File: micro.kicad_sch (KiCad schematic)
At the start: 0 parts

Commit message: added mcu to schematics
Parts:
- added U1: ~, symbol sumo-robot-symbols:MSP430G2553IPW28
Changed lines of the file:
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@@
 	(generator_version "9.0")
 	(paper "A4")
+	(symbol
+		(lib_id "sumo-robot-symbols:MSP430G2553IPW28")
+		(at 137.16 102.87 0)
+		(unit 1)
+		(exclude_from_sim no)
+		(in_bom yes)
+		(on_board yes)
+		(dnp no)
+		(fields_autoplaced yes)
+		(property "Reference" "U1"
+			(at 158.115 60.96 0)
+			(effects
+				(font
+					(size 1.27 1.27)
+				)
+			)
+		)
+		(property "Value" "~"
+			(at 158.115 63.5 0)
+			(effects
+				(font
+					(size 1.27 1.27)
+				)
+			)
+		)
+		(property "Footprint" ""
+			(at 137.16 102.87 0)
+			(effects
+				(font
+					(size 1.27 1.27)
+				)
+				(hide yes)
+			)
+		)
+		(property "Datasheet" ""
+			(at 137.16 102.87 0)
+			(effects
+				(font
+					(size 1.27 1.27)
+				)
+				(hide yes)
+			)
+		)
+		(property "Description" ""
+			(at 137.16 102.87 0)
+			(effects
+				(font
+					(size 1.27 1.27)
+				)
+				(hide yes)
+			)
+		)
+		(pin "5"
+		)
+		(pin "8"
+		)
+		(pin "3"
+		)
+		(pin "1"
+		)
+		(pin "7"
+		)
+		(pin "20"
+		)
+		(pin "16"
+		)
+		(pin "4"
+		)
+		(pin "26"
+		)
+		(pin "14"
+		)
+		(pin "9"
+		)
+		(pin "25"
+		)
+		(pin "24"
+		)
+		(pin "12"
+		)
+		(pin "2"
+		)
+		(pin "6"
+		)
+		(pin "13"
+		)
+		(pin "28"
+		)
+		(pin "27"
+		)
+		(pin "22"
+		)
+		(pin "19"
+		)
+		(pin "18"
+		)
+		(pin "17"
+		)
+		(pin "23"
+		)
+		(pin "21"
+		)
+		(pin "11"
+		)
+		(pin "10"
+		)
+		(pin "15"
+		)
+		(instances
+			(project ""
+				(path "/f283bc71-7763-4093-b75c-cbe2f5868c12/9428f158-f7fc-4e4a-b97b-e16df299d57c"
+					(reference "U1")
+					(unit 1)
+				)
+			)
+		)
+	)
 )

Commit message: updated poer and range sensor scheamtics
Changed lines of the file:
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@@
 	(generator_version "9.0")
 	(paper "A4")
+	(text_box "There would be some flags coming from the pins to indicate that sensors are active "
+		(exclude_from_sim no)
+		(at 96.52 40.64 0)
+		(size 19.05 17.78)
+		(margins 0.9525 0.9525 0.9525 0.9525)
+		(stroke
+			(width 0)
+			(type solid)
+		)
+		(fill
+			(type none)
+		)
+		(effects
+			(font
+				(size 1.27 1.27)
+			)
+			(justify left top)
+		)
+	)
 	(symbol
 		(lib_id "sumo-robot-symbols:MSP430G2553IPW28")
@@
 		(on_board yes)
 		(dnp no)
-		(fields_autoplaced yes)
 		(property "Reference" "U1"
-			(at 158.115 60.96 0)
+			(at 157.988 63.246 0)
 			(effects
 				(font

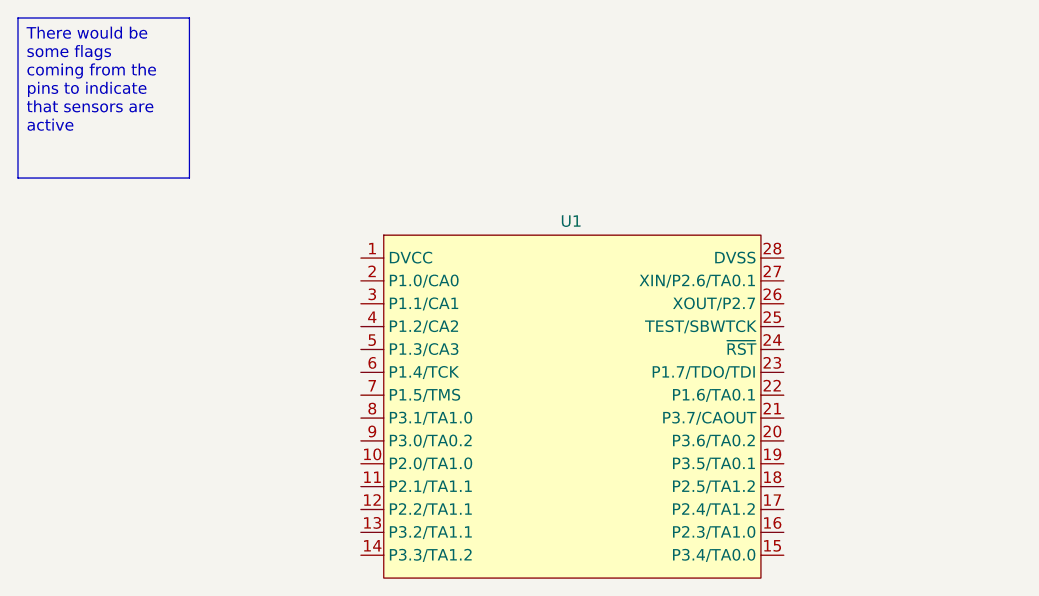
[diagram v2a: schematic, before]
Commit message: added I2C lines
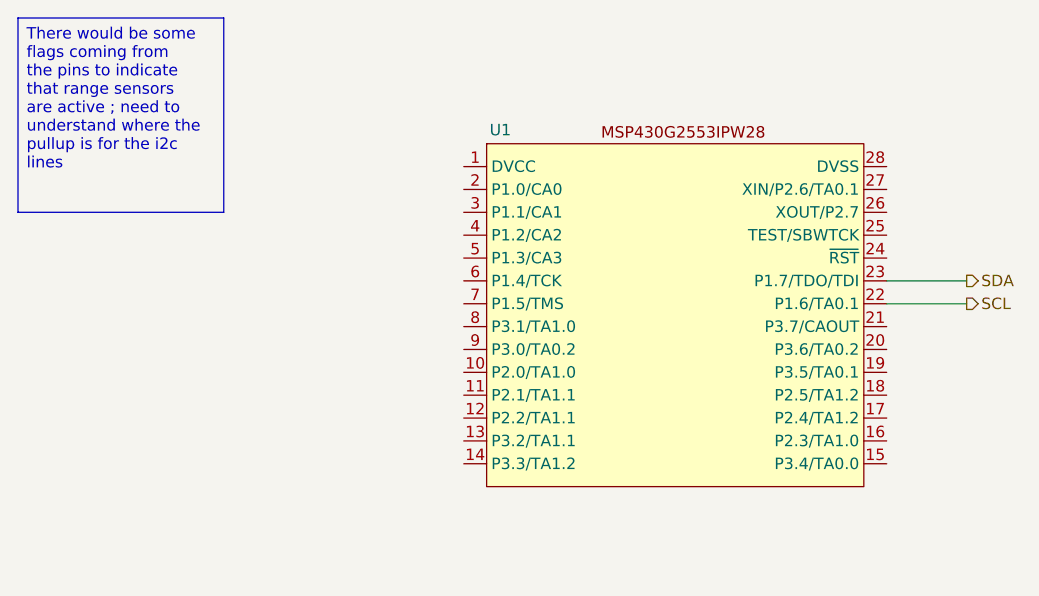
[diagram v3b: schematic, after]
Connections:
- net SCL: now reaches U1.22 (P1.6/TA0.1)
- net SDA: now reaches U1.23 (P1.7/TDO/TDI)
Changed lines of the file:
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@@
 	(generator_version "9.0")
 	(paper "A4")
-	(text_box "There would be some flags coming from the pins to indicate that sensors are active "
+	(text_box "There would be some flags coming from the pins to indicate that range sensors are active ; need to understand where the pullup is for the i2c lines "
 		(exclude_from_sim no)
 		(at 96.52 40.64 0)
-		(size 19.05 17.78)
+		(size 22.86 21.59)
 		(margins 0.9525 0.9525 0.9525 0.9525)
 		(stroke
@@
 		)
 	)
+	(wire
+		(pts
+			(xy 193.04 72.39) (xy 201.93 72.39)
+		)
+		(stroke
+			(width 0)
+			(type default)
+		)
+	)
+	(wire
+		(pts
+			(xy 193.04 69.85) (xy 201.93 69.85)
+		)
+		(stroke
+			(width 0)
+			(type default)
+		)
+	)
+	(hierarchical_label "SCL"
+		(shape output)
+		(at 201.93 72.39 0)
+		(effects
+			(font
+				(size 1.27 1.27)
+			)
+			(justify left)
+		)
+	)
+	(hierarchical_label "SDA"
+		(shape output)
+		(at 201.93 69.85 0)
+		(effects
+			(font
+				(size 1.27 1.27)
+			)
+			(justify left)
+		)
+	)
 	(symbol
 		(lib_id "sumo-robot-symbols:MSP430G2553IPW28")
-		(at 137.16 102.87 0)
+		(at 148.59 92.71 0)
 		(unit 1)
 		(exclude_from_sim no)
@@
 		(dnp no)
 		(property "Reference" "U1"
-			(at 157.988 63.246 0)
+			(at 150.114 53.086 0)
 			(effects
 				(font
@@
 		)
 		(property "Value" "~"
-			(at 158.115 63.5 0)
+			(at 169.545 50.8 0)
 			(effects
 				(font
@@
 		)
 		(property "Footprint" ""
-			(at 137.16 102.87 0)
+			(at 148.59 92.71 0)
 			(effects
 				(font
@@
 		)
 		(property "Datasheet" ""
-			(at 137.16 102.87 0)
+			(at 148.59 92.71 0)
 			(effects
 				(font
@@
 		)
 		(property "Description" ""
-			(at 137.16 102.87 0)
+			(at 148.59 92.71 0)
 			(effects
 				(font
@@
 			)
 		)
-		(pin "5"
+		(pin "1"
+		)
+		(pin "24"
+		)
+		(pin "14"
+		)
+		(pin "6"
+		)
+		(pin "18"
+		)
+		(pin "16"
+		)
+		(pin "7"
+		)
+		(pin "9"
 		)
 		(pin "8"
 		)
+		(pin "4"
+		)
+		(pin "13"
+		)
+		(pin "27"
+		)
+		(pin "5"
+		)
+		(pin "10"
+		)
+		(pin "11"
+		)
+		(pin "26"
+		)
+		(pin "12"
+		)
+		(pin "28"
+		)
+		(pin "25"
+		)
 		(pin "3"
 		)
-		(pin "1"
+		(pin "23"
 		)
-		(pin "7"
+		(pin "2"
+		)
+		(pin "22"
+		)
+		(pin "21"
 		)
 		(pin "20"
 		)
-		(pin "16"
-		)
-		(pin "4"
-		)
-		(pin "26"
-		)
-		(pin "14"
-		)
-		(pin "9"
-		)
-		(pin "25"
-		)
-		(pin "24"
-		)
-		(pin "12"
-		)
-		(pin "2"
-		)
-		(pin "6"
-		)
-		(pin "13"
-		)
-		(pin "28"
-		)
-		(pin "27"
-		)
-		(pin "22"
-		)
 		(pin "19"
-		)
-		(pin "18"
 		)
 		(pin "17"
 		)
-		(pin "23"
-		)
-		(pin "21"
-		)
-		(pin "11"
-		)
-		(pin "10"
-		)
 		(pin "15"

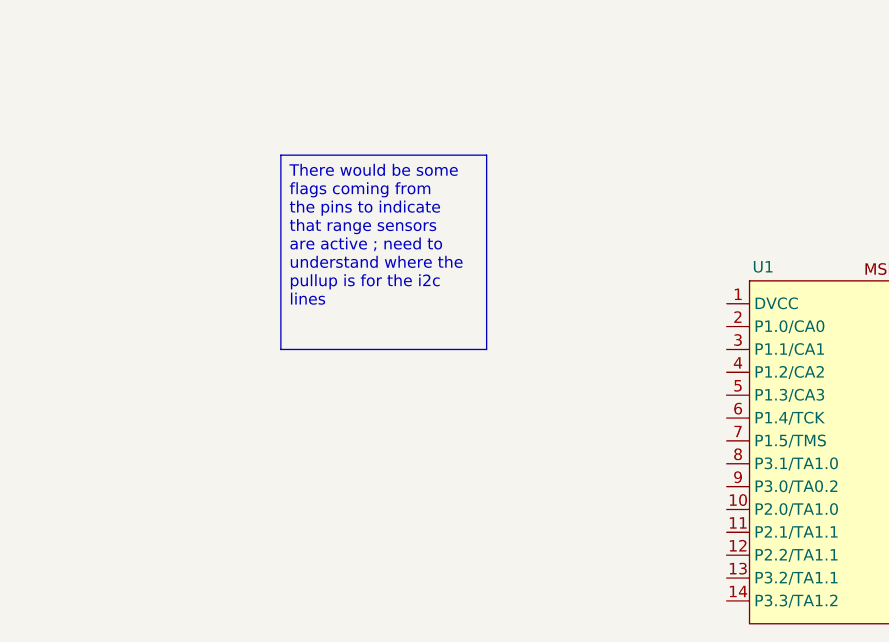
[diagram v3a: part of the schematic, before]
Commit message: added IR receiver circuit
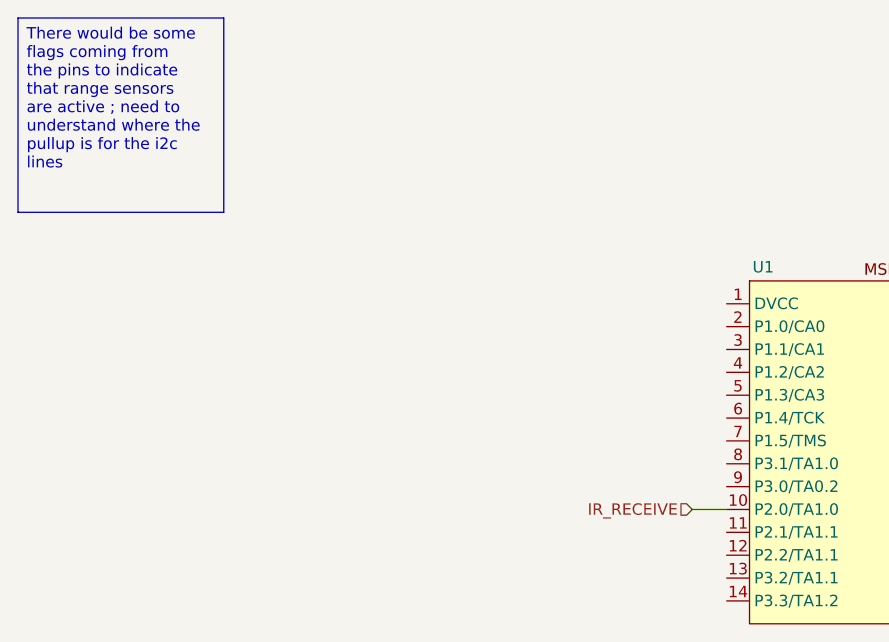
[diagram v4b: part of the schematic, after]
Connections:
- net IR_RECEIVE: now reaches U1.10 (P2.0/TA1.0)
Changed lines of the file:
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@@
 	(text_box "There would be some flags coming from the pins to indicate that range sensors are active ; need to understand where the pullup is for the i2c lines "
 		(exclude_from_sim no)
-		(at 96.52 40.64 0)
+		(at 67.31 25.4 0)
 		(size 22.86 21.59)
 		(margins 0.9525 0.9525 0.9525 0.9525)
@@
 			)
 			(justify left top)
+		)
+	)
+	(wire
+		(pts
+			(xy 142.24 80.01) (xy 146.05 80.01)
+		)
+		(stroke
+			(width 0)
+			(type default)
 		)
 	)
@@
 		)
 	)
+	(hierarchical_label "IR_RECEIVE"
+		(shape input)
+		(at 142.24 80.01 180)
+		(effects
+			(font
+				(size 1.27 1.27)
+			)
+			(justify right)
+		)
+	)

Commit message: added more details to schematics
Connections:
- net LD_FRONT_LEFT: now reaches U1.5 (P1.3/CA3)
- net LD_BACK_LEFT: now reaches U1.6 (P1.4/TCK)
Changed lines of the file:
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@@
 	(wire
 		(pts
-			(xy 193.04 72.39) (xy 201.93 72.39)
+			(xy 142.24 67.31) (xy 146.05 67.31)
 		)
 		(stroke
@@
 	(wire
 		(pts
-			(xy 193.04 69.85) (xy 201.93 69.85)
+			(xy 193.04 72.39) (xy 199.39 72.39)
 		)
 		(stroke
 			(width 0)
 			(type default)
+		)
+	)
+	(wire
+		(pts
+			(xy 142.24 69.85) (xy 146.05 69.85)
+		)
+		(stroke
+			(width 0)
+			(type default)
+		)
+	)
+	(wire
+		(pts
+			(xy 193.04 69.85) (xy 199.39 69.85)
+		)
+		(stroke
+			(width 0)
+			(type default)
+		)
+	)
+	(hierarchical_label "LD_FRONT_LEFT"
+		(shape input)
+		(at 142.24 67.31 180)
+		(effects
+			(font
+				(size 1.27 1.27)
+			)
+			(justify right)
 		)
 	)
@@
 	(hierarchical_label "SCL"
 		(shape output)
-		(at 201.93 72.39 0)
+		(at 199.39 72.39 0)
+		(effects
+			(font
+				(size 1.27 1.27)
+			)
+			(justify left)
+		)
+	)
+	(hierarchical_label "LD_BACK_RIGHT"
+		(shape input)
+		(at 245.11 146.05 90)
 		(effects
 			(font
@@
 	(hierarchical_label "SDA"
 		(shape output)
-		(at 201.93 69.85 0)
+		(at 199.39 69.85 0)
 		(effects
 			(font
@@
 		)
 	)
+	(hierarchical_label "LD_FRONT_RIGHT"
+		(shape input)
+		(at 184.15 144.78 90)
+		(effects
+			(font
+				(size 1.27 1.27)
+			)
+			(justify left)
+		)
+	)
+	(hierarchical_label "LD_BACK_LEFT"
+		(shape input)
+		(at 142.24 69.85 180)
+		(effects
+			(font
+				(size 1.27 1.27)
+			)
+			(justify right)
+		)
+	)

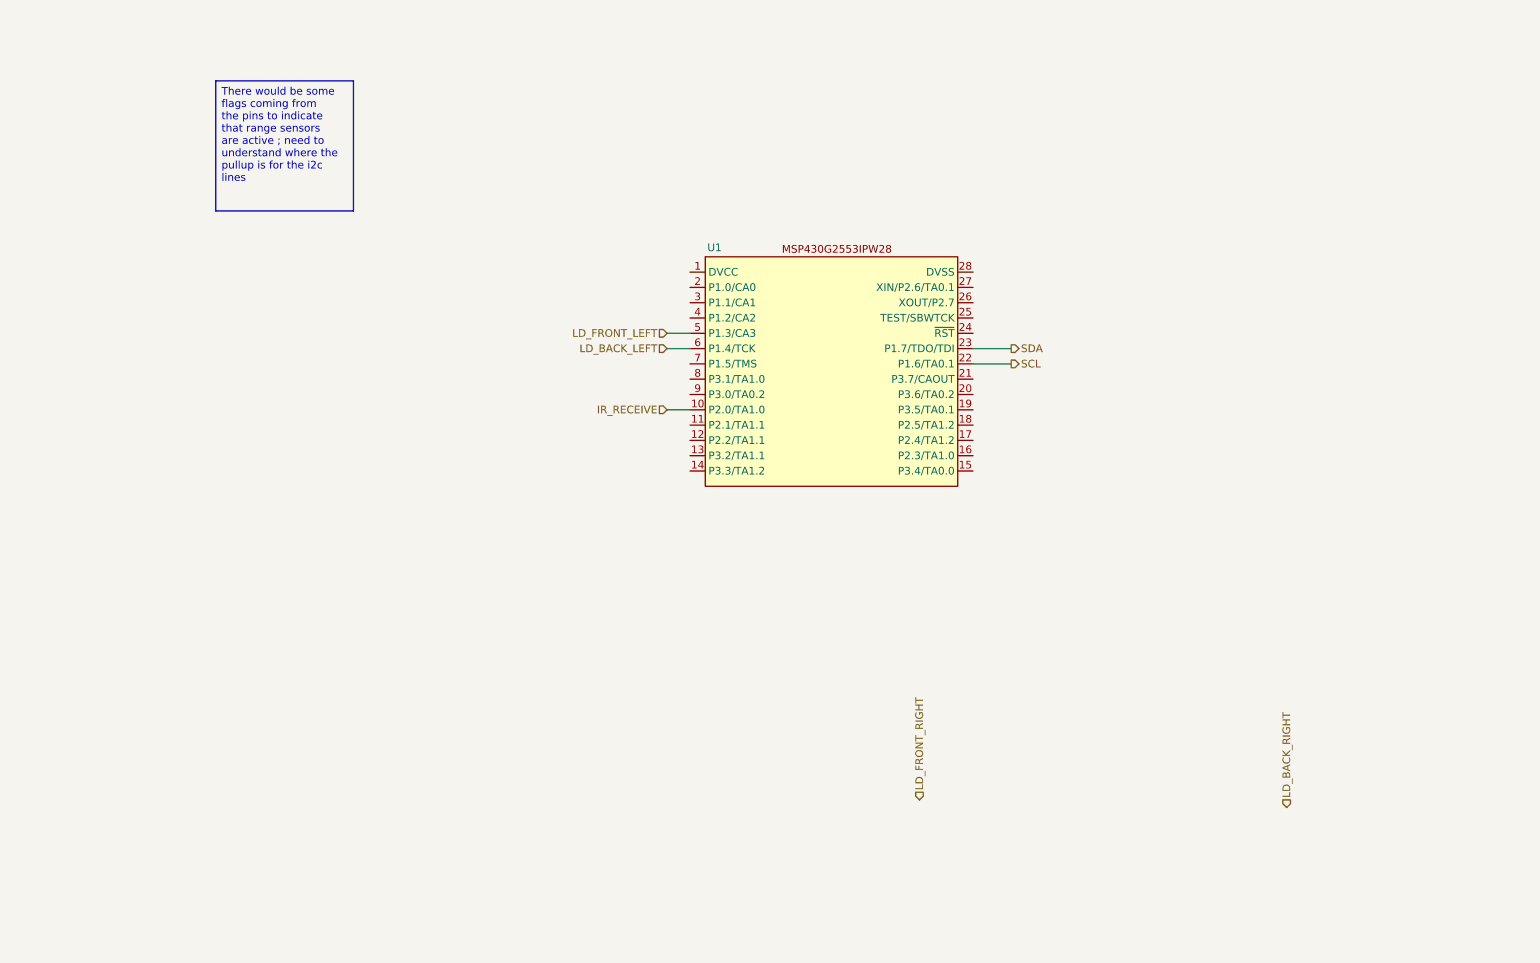
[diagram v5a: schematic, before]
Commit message: updated logic for MCU
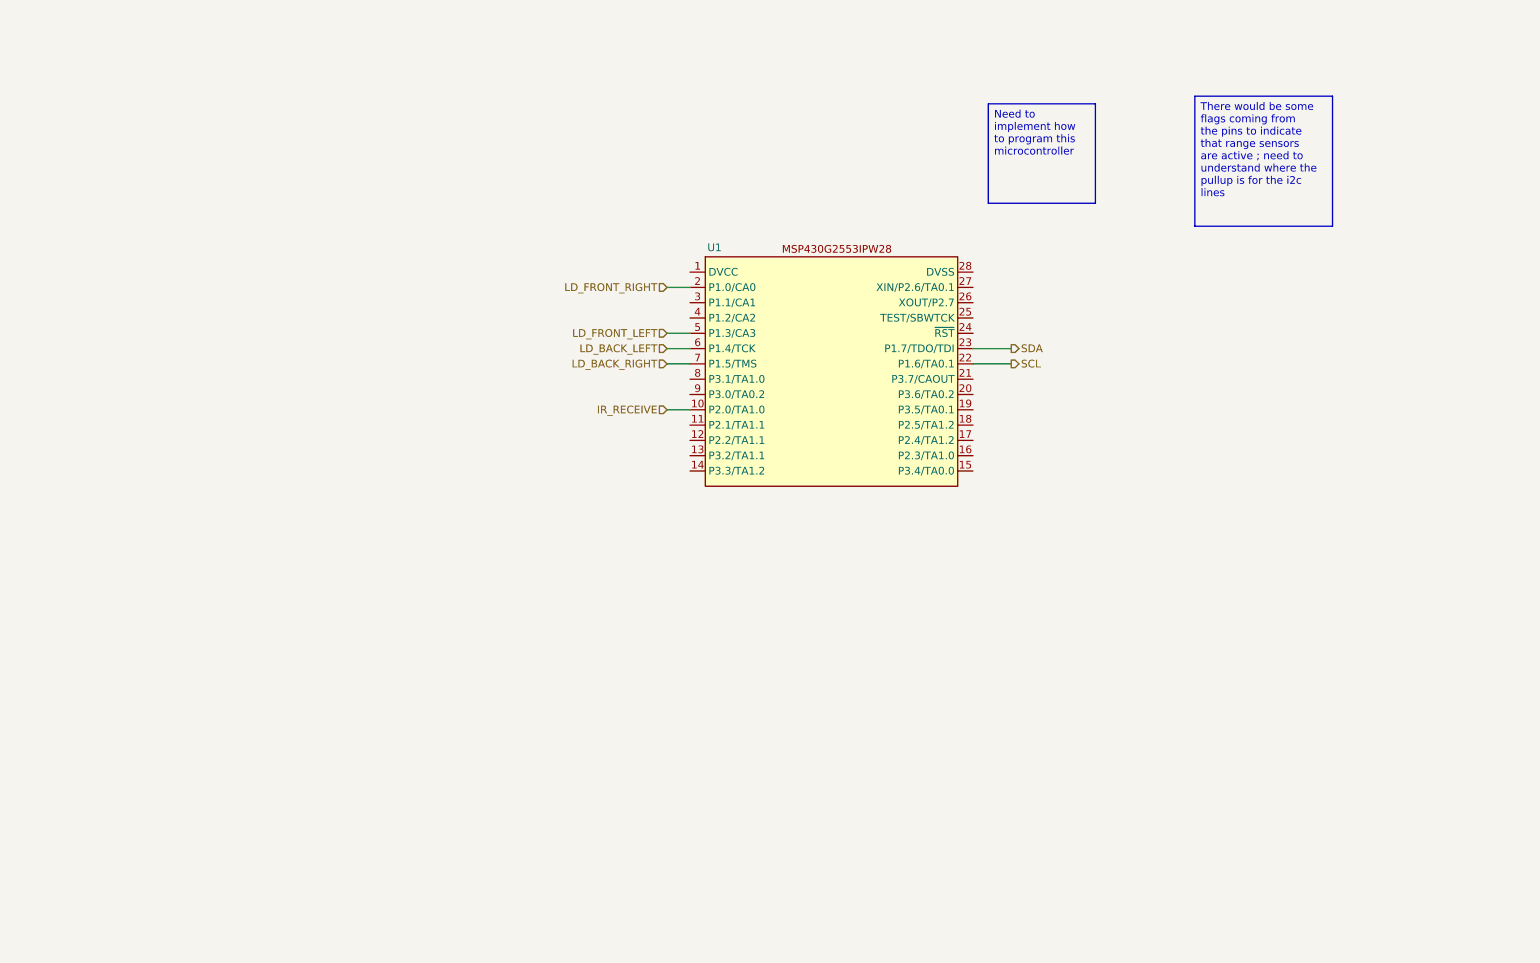
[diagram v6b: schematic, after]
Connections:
- net LD_BACK_RIGHT: now also U1.7 (P1.5/TMS)
- net LD_FRONT_RIGHT: now also U1.2 (P1.0/CA0)
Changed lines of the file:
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@@
 	(text_box "There would be some flags coming from the pins to indicate that range sensors are active ; need to understand where the pullup is for the i2c lines "
 		(exclude_from_sim no)
-		(at 67.31 25.4 0)
+		(at 229.87 27.94 0)
 		(size 22.86 21.59)
+		(margins 0.9525 0.9525 0.9525 0.9525)
+		(stroke
+			(width 0)
+			(type solid)
+		)
+		(fill
+			(type none)
+		)
+		(effects
+			(font
+				(size 1.27 1.27)
+			)
+			(justify left top)
+		)
+	)
+	(text_box "Need to implement how to program this microcontroller "
+		(exclude_from_sim no)
+		(at 195.58 29.21 0)
+		(size 17.78 16.51)
 		(margins 0.9525 0.9525 0.9525 0.9525)
 		(stroke
@@
 		(pts
 			(xy 142.24 80.01) (xy 146.05 80.01)
+		)
+		(stroke
+			(width 0)
+			(type default)
+		)
+	)
+	(wire
+		(pts
+			(xy 142.24 59.69) (xy 146.05 59.69)
 		)
 		(stroke
@@
 		(pts
 			(xy 142.24 69.85) (xy 146.05 69.85)
+		)
+		(stroke
+			(width 0)
+			(type default)
+		)
+	)
+	(wire
+		(pts
+			(xy 142.24 72.39) (xy 146.05 72.39)
 		)
 		(stroke
@@
 	(hierarchical_label "LD_BACK_RIGHT"
 		(shape input)
-		(at 245.11 146.05 90)
+		(at 142.24 72.39 180)
 		(effects
 			(font
 				(size 1.27 1.27)
 			)
-			(justify left)
+			(justify right)
 		)
 	)
@@
 	(hierarchical_label "LD_FRONT_RIGHT"
 		(shape input)
-		(at 184.15 144.78 90)
+		(at 142.24 59.69 180)
 		(effects
 			(font
 				(size 1.27 1.27)
 			)
-			(justify left)
+			(justify right)
 		)
 	)

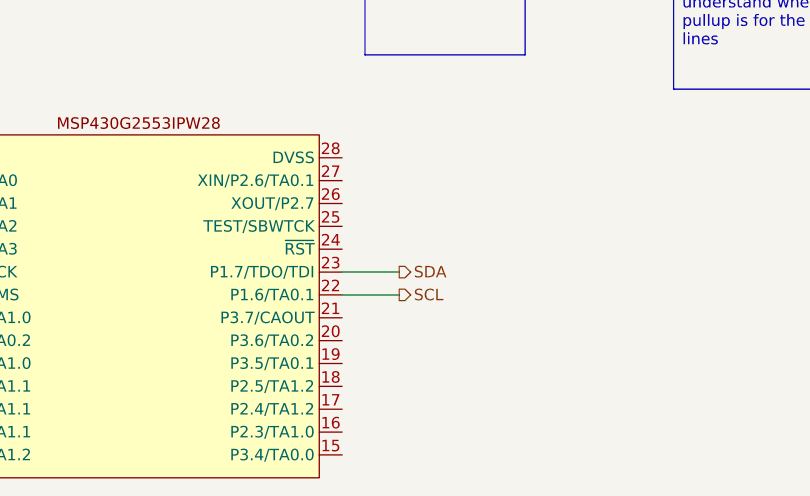
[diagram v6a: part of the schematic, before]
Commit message: started adding DC Motor controller logic
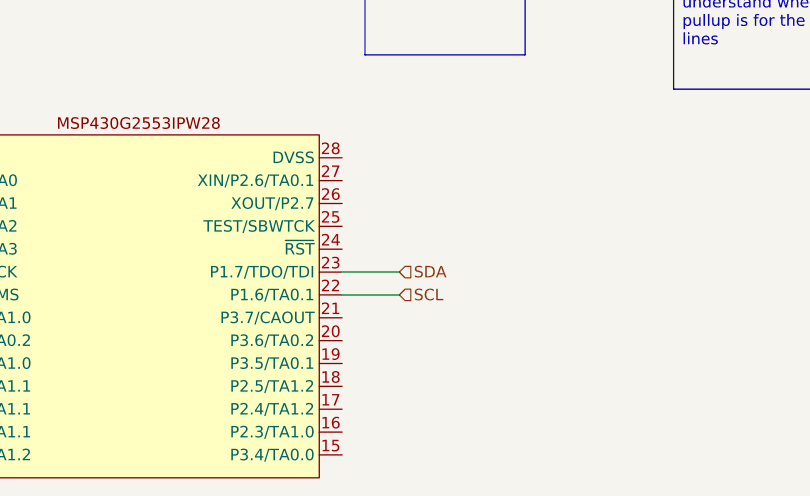
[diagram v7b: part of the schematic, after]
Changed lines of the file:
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@@
 	)
 	(hierarchical_label "SCL"
-		(shape output)
+		(shape input)
 		(at 199.39 72.39 0)
 		(effects
@@
 	)
 	(hierarchical_label "SDA"
-		(shape output)
+		(shape input)
 		(at 199.39 69.85 0)
 		(effects
